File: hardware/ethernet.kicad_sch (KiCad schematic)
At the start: 92 parts, among them J5 USB_C_Receptacle, Q1 BSS138, Q2 BSS138, U14 KSZ9031RNXCA, U4 GateMate-CCGM1A1, X1 ECS-2520MV-250-xx

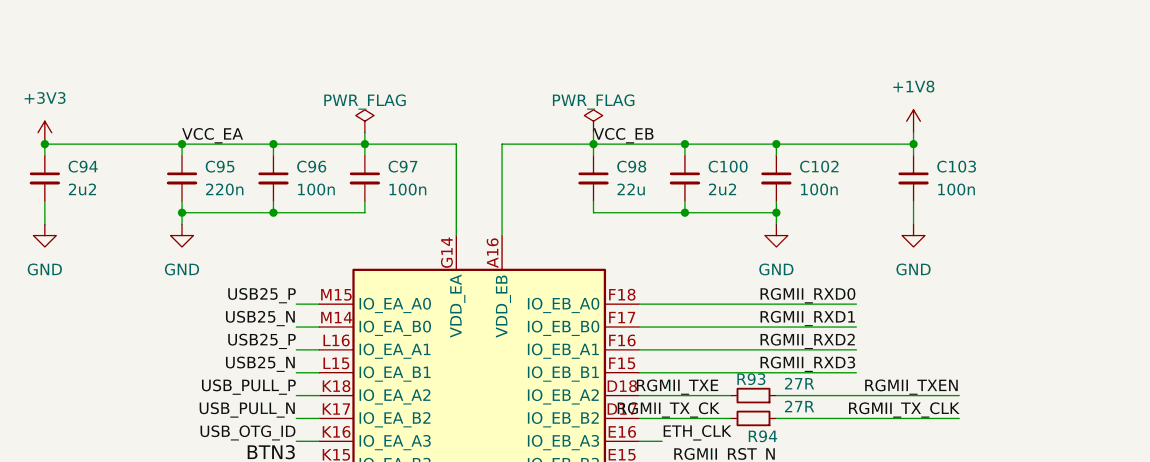
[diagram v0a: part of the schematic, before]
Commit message: power: removed rc filters from gpio domains
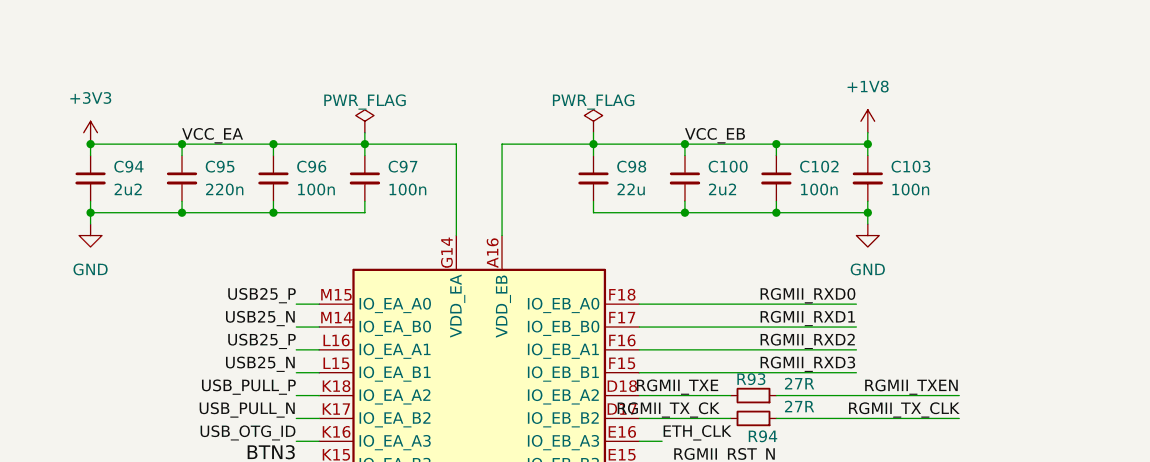
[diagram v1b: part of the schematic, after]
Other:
- moved on the sheet: C103, C94

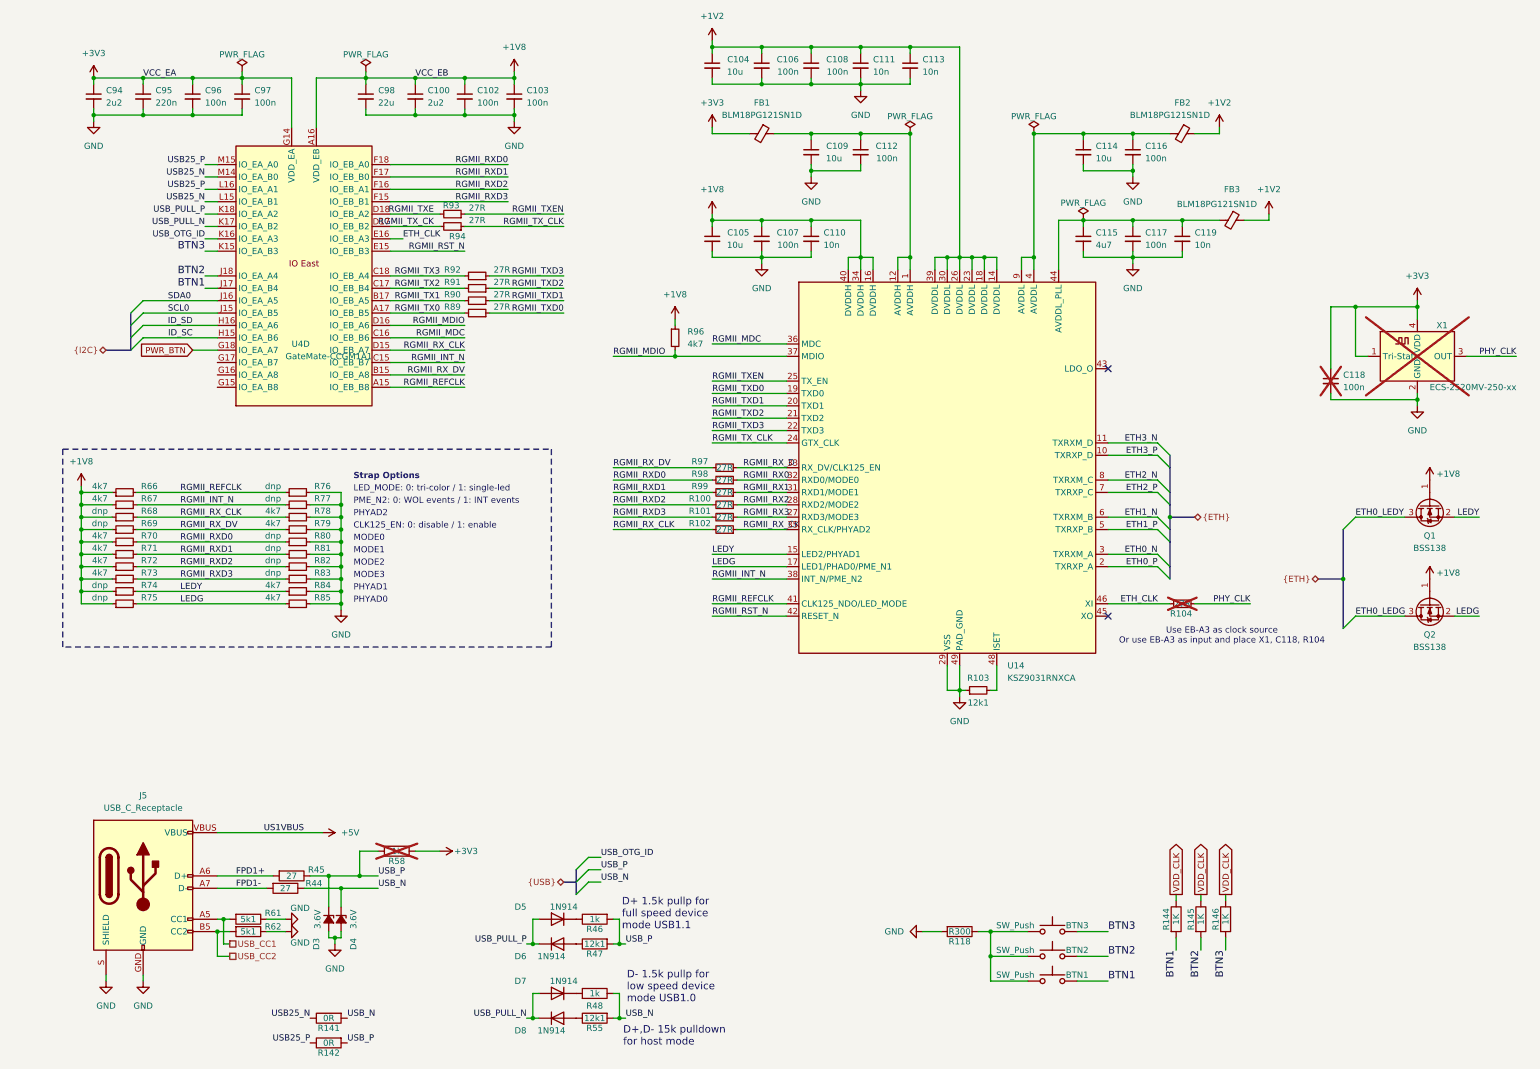
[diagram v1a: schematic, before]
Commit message: ethernet: remove push buttons
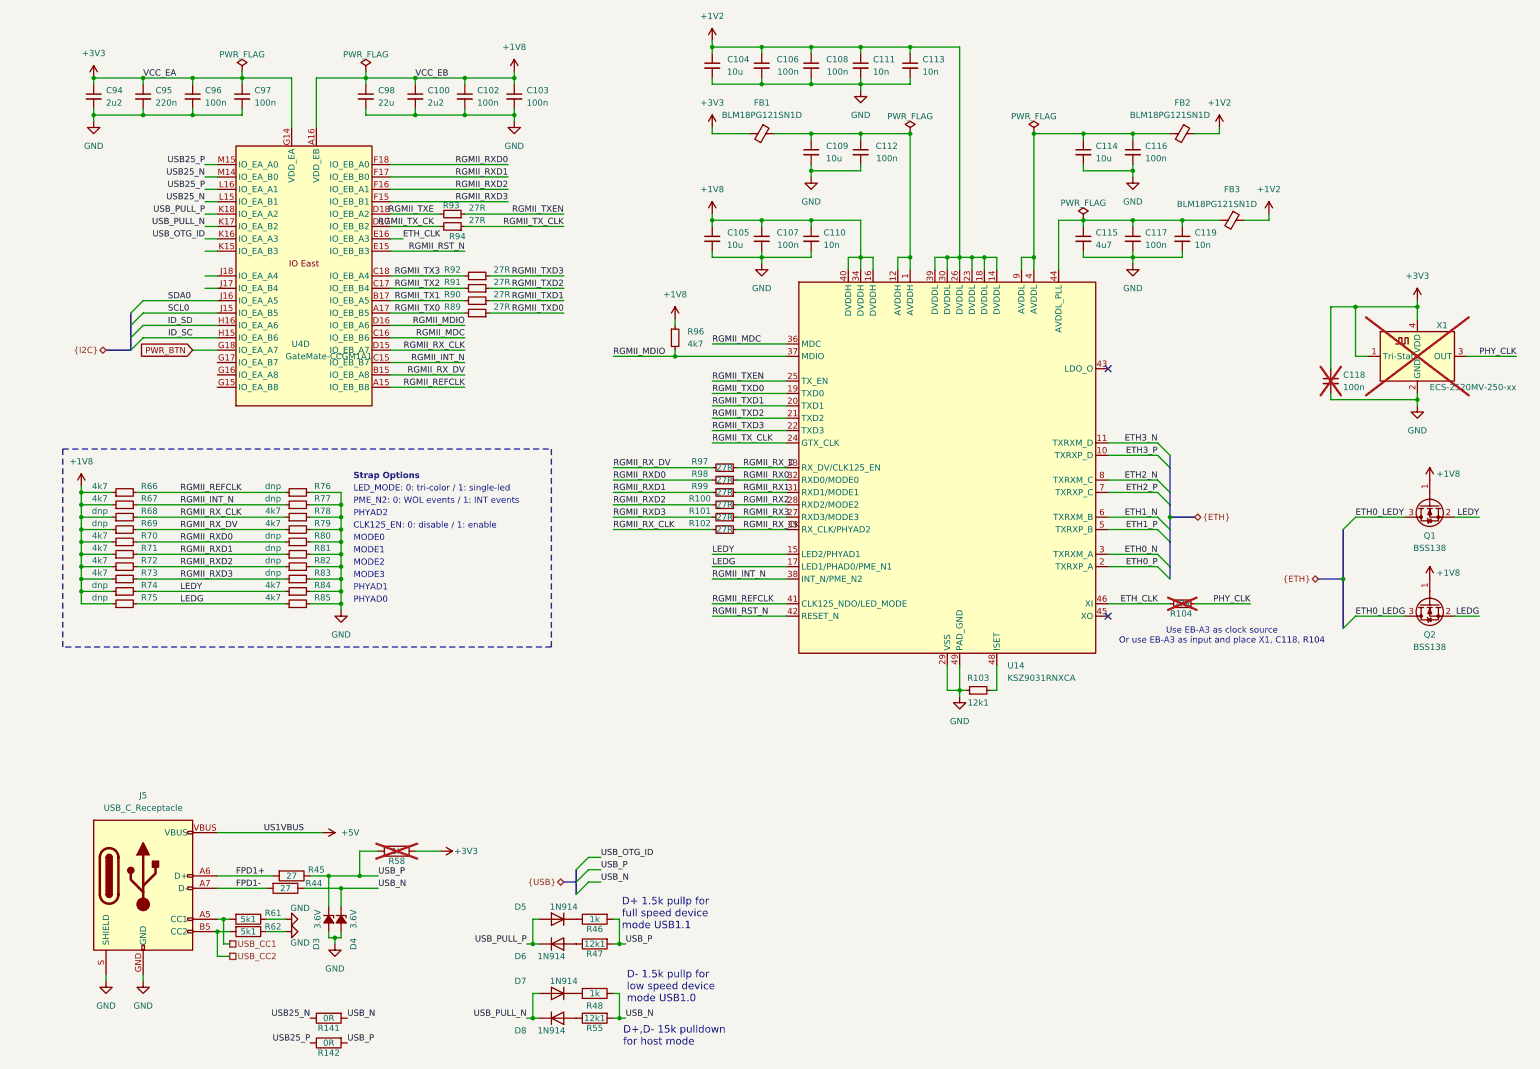
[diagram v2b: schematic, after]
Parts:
- removed BTN1, BTN2, BTN3: SW_Push, Switch_EVPAA:Switch_EVPAA, symbol Switch:SW_Push
- removed R118: R300, Resistor_SMD:R_0402_1005Metric, symbol Device:R
- removed R144, R145, R146: 1K, Resistor_SMD:R_0402_1005Metric, symbol Device:R
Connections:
- net BTN1: no longer names the net of U4.J17 (IO_EA_B4)
- net BTN2: no longer names the net of U4.J18 (IO_EA_A4)
- net BTN3: no longer names the net of U4.K15 (IO_EA_B3)

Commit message: ethernet: simplify usb interface
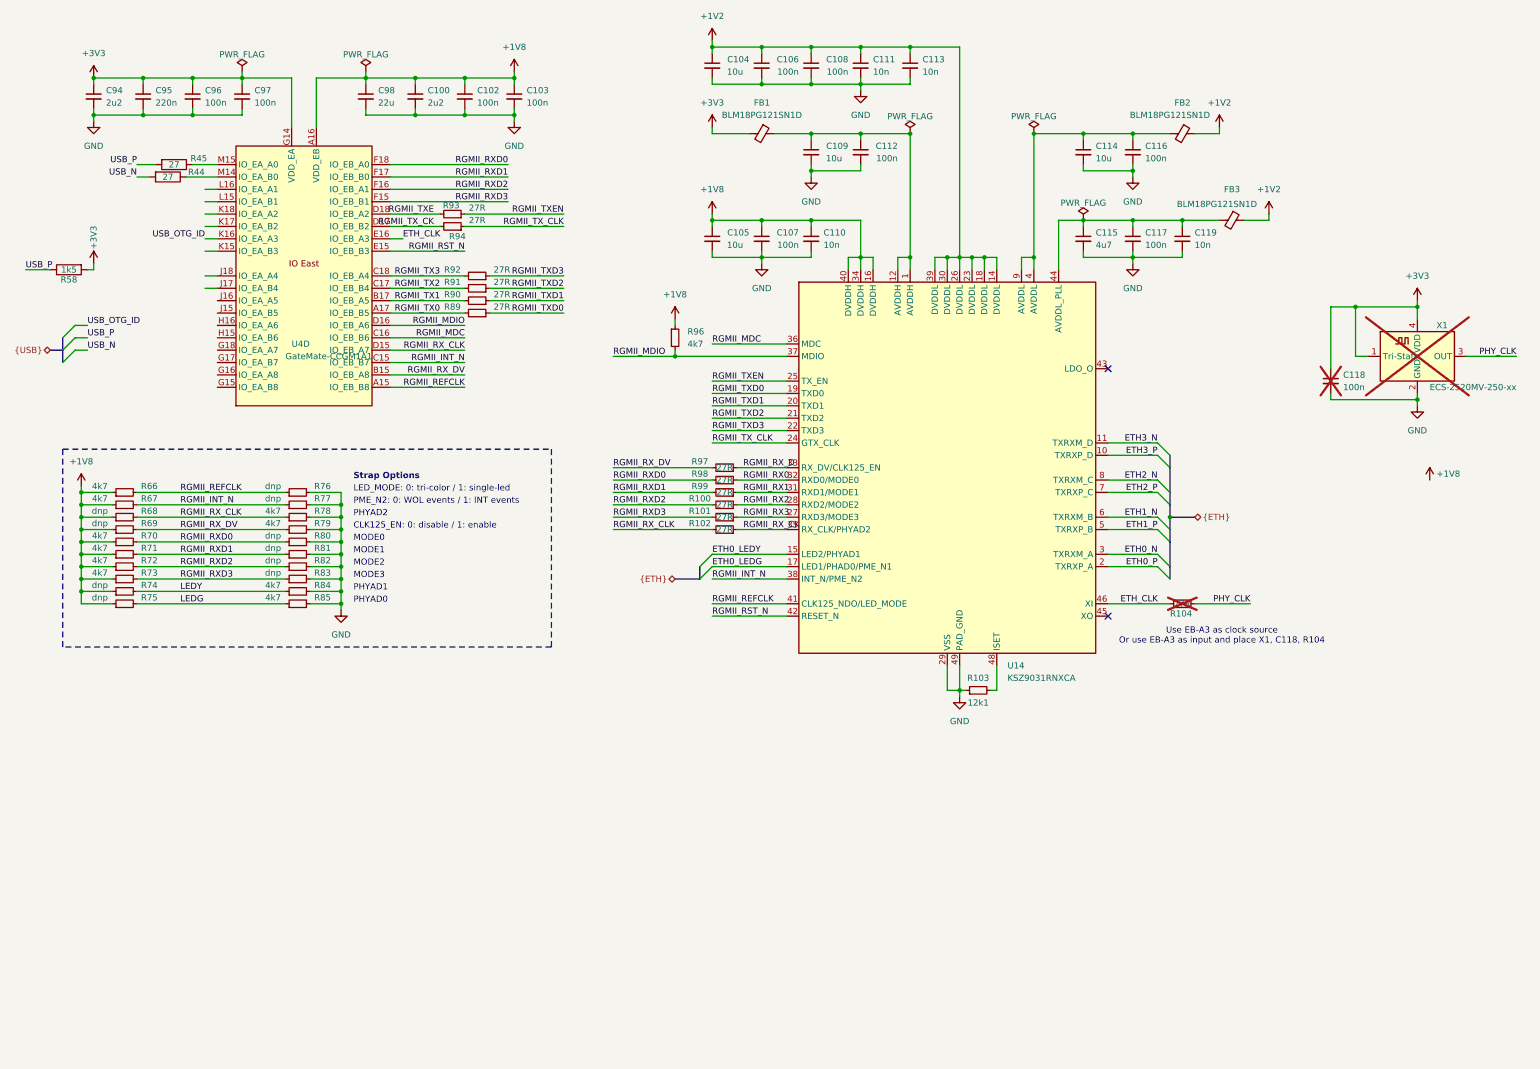
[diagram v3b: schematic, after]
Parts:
- removed D3, D4: 3.6V, Diode_SMD:D_SOD-523, symbol Device:D_Zener_Small_Filled
- removed D5, D6, D7, D8: 1N914, Diode_SMD:D_SOD-523, symbol Device:D
- removed J5: USB_C_Receptacle, ulx5m-gs:USB-C_16, symbol SparkFun-Connector:USB_C_Receptacle
- removed Q1, Q2: BSS138, Package_TO_SOT_SMD:SOT-523, symbol Transistor_FET:BSS138
- removed R141, R142: 0R, Resistor_SMD:R_0402_1005Metric, symbol Device:R
- removed R46, R48: 1k, Resistor_SMD:R_0402_1005Metric, symbol Device:R
- removed R47, R55: 12k1, Resistor_SMD:R_0402_1005Metric, symbol Device:R
- removed R61, R62: 5k1, Resistor_SMD:R_0402_1005Metric, symbol Device:R
- R58: value 1k -> 1k5; now fitted
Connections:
- net FPD1+ is gone; now on net USB_P: R45.2
- net FPD1- is gone; now on net USB_N: R44.2
- net ETH0_LEDG: now also U14.17 (LED1/PHAD0/PME_N1)
- net ETH0_LEDY: now also U14.15 (LED2/PHYAD1)
- net LEDG: no longer U14.17 (LED1/PHAD0/PME_N1)
- net LEDY: no longer U14.15 (LED2/PHYAD1)
- net USB_N: no longer R44.1
- net USB_P: no longer R45.1
- net ID_SC: no longer names the net of U4.H15 (IO_EA_B6)
- net ID_SD: no longer names the net of U4.H16 (IO_EA_A6)
- net PWR_BTN: no longer names the net of U4.G18 (IO_EA_A7)
- net SCL0: no longer names the net of U4.J15 (IO_EA_B5)
- net SDA0: no longer names the net of U4.J16 (IO_EA_A5)
- net USB25_N: no longer names the net of U4.L15 (IO_EA_B1)
- net USB25_N: no longer U4.M14 (IO_EA_B0)
- net USB25_P: no longer names the net of U4.L16 (IO_EA_A1)
- net USB25_P: no longer U4.M15 (IO_EA_A0)
- net USB_PULL_N: no longer names the net of U4.K17 (IO_EA_B2)
- net USB_PULL_P: no longer names the net of U4.K18 (IO_EA_A2)
- new net: R44.1, U4.M14 (IO_EA_B0)
- new net: R45.1, U4.M15 (IO_EA_A0)
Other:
- note removed: "D+ 1.5k pullp for full speed device mode USB1.1"
- note removed: "D+,D- 15k pulldown for host mode"
- note removed: "D- 1.5k pullp for low speed device mode USB1.0"
- moved on the sheet: R44, R45
